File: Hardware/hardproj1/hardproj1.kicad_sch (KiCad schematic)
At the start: 4 parts, among them J1 Conn_01x02_Male, SW1 SW_Push

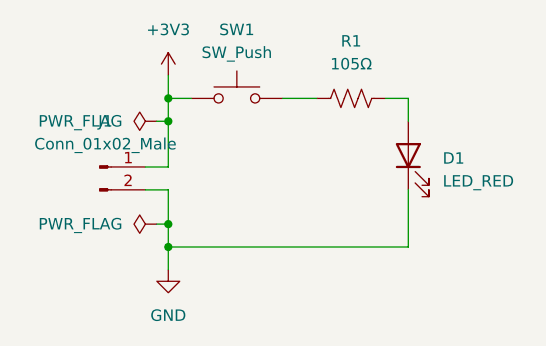
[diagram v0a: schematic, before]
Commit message: Fixed wrong connector schematic symbol.
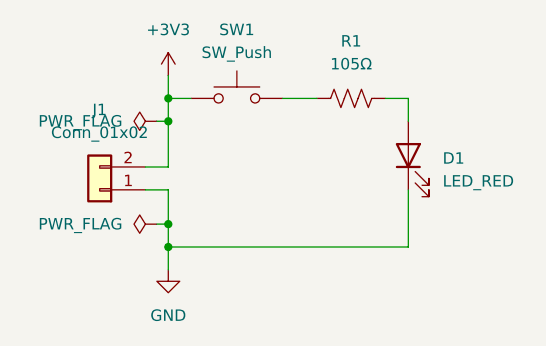
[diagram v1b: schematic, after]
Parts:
- removed J1: Conn_01x02_Male, Connector_Molex:Molex_KK-254_AE-6410-02A_1x02_P2.54mm_Vertical, symbol Connector:Conn_01x02_Male
- added J1: Conn_01x02, Connector_Molex:Molex_KK-254_AE-6410-02A_1x02_P2.54mm_Vertical, symbol Connector_Generic:Conn_01x02
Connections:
- net +3V3: now also J1.2 (Pin_2)
- net GND: now also J1.1 (Pin_1)
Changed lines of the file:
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@@
-	)
-	(symbol
-		(lib_id "Connector:Conn_01x02_Male")
-		(at 80.01 102.87 0)
-		(unit 1)
-		(exclude_from_sim no)
-		(in_bom yes)
-		(on_board yes)
-		(dnp no)
-		(fields_autoplaced yes)
-		(property "Reference" "J1"
-			(at 80.645 97.79 0)
-			(effects
-				(font
-					(size 1.27 1.27)
-				)
-			)
-		)
-		(property "Value" "Conn_01x02_Male"
-			(at 80.645 100.33 0)
-			(effects
-				(font
-					(size 1.27 1.27)
-				)
-			)
-		)
-		(property "Footprint" "Connector_Molex:Molex_KK-254_AE-6410-02A_1x02_P2.54mm_Vertical"
-			(at 80.01 102.87 0)
-			(effects
-				(font
-					(size 1.27 1.27)
-				)
-				(hide yes)
-			)
-		)
-		(property "Datasheet" "https://www.molex.com/en-us/products/part-detail/22272021?display=pdf"
-			(at 80.01 102.87 0)
-			(effects
-				(font
-					(size 1.27 1.27)
-				)
-				(hide yes)
-			)
-		)
-		(property "Description" "Generic connector, single row, 01x02, script generated (kicad-library-utils/schlib/autogen/connector/)"
-			(at 80.01 102.87 0)
-			(effects
-				(font
-					(size 1.27 1.27)
-				)
-				(hide yes)
-			)
-		)
-		(property "MPN" "22272021"
-			(at 80.01 102.87 0)
-			(effects
-				(font
-					(size 1.27 1.27)
-				)
-				(hide yes)
-			)
-		)
-		(property "Notes" ""
-			(at 80.01 102.87 0)
-			(effects
-				(font
-					(size 1.27 1.27)
-				)
-				(hide yes)
-			)
-		)
-		(pin "2"
-		)
-		(pin "1"
-		)
-		(instances
-			(project "hardproj1"
-				(path "/1e1b062d-fad0-427c-a622-c5b8a80b5268"
-					(reference "J1")
-					(unit 1)
-				)
-			)
-		)
 	)
 	(symbol
@@
 					(unit 1)
 				)
+			)
+		)
+	)
+	(symbol
+		(lib_id "Connector_Generic:Conn_01x02")
+		(at 80.01 105.41 180)
+		(unit 1)
+		(exclude_from_sim no)
+		(in_bom yes)
+		(on_board yes)
+		(dnp no)
+		(fields_autoplaced yes)
+		(property "Reference" "J1"
+			(at 80.01 96.52 0)
+			(effects
+				(font
+					(size 1.27 1.27)
+				)
+			)
+		)
+		(property "Value" "Conn_01x02"
+			(at 80.01 99.06 0)
+			(effects
+				(font
+					(size 1.27 1.27)
+				)
+			)
+		)
+		(property "Footprint" "Connector_Molex:Molex_KK-254_AE-6410-02A_1x02_P2.54mm_Vertical"
+			(at 80.01 105.41 0)
+			(effects
+				(font
+					(size 1.27 1.27)
+				)
+				(hide yes)
+			)
+		)
+		(property "Datasheet" "https://www.molex.com/content/dam/molex/molex-dot-com/products/automated/en-us/salesdrawingpdf/641/6410/022272021_sd.pdf?inline"
+			(at 80.01 105.41 0)
+			(effects
+				(font
+					(size 1.27 1.27)
+				)
+				(hide yes)
+			)
+		)
+		(property "Description" "Generic connector, single row, 01x02, script generated (kicad-library-utils/schlib/autogen/connector/)"
+			(at 80.01 105.41 0)
+			(effects
+				(font
+					(size 1.27 1.27)
+				)
+				(hide yes)
+			)
+		)
+		(property "MPN" "AE-6410-02A"
+			(at 80.01 105.41 0)
+			(effects
+				(font
+					(size 1.27 1.27)
+				)
+				(hide yes)
+			)
+		)
+		(pin "1"
+		)
+		(pin "2"
+		)
+		(instances
+			(project "hardproj1"
+				(path "/1e1b062d-fad0-427c-a622-c5b8a80b5268"
+					(reference "J1")
+					(unit 1)
+				)
